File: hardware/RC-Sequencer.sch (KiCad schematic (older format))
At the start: 18 parts, among them J1 CH3, J2 Conn_02x05_Odd_Even, J3 Conn_02x04_Odd_Even, Q1 AO3400, Q2 AO3400, Q3 AO3400, Q4 AO3400, U1 ATtiny44-20SSU

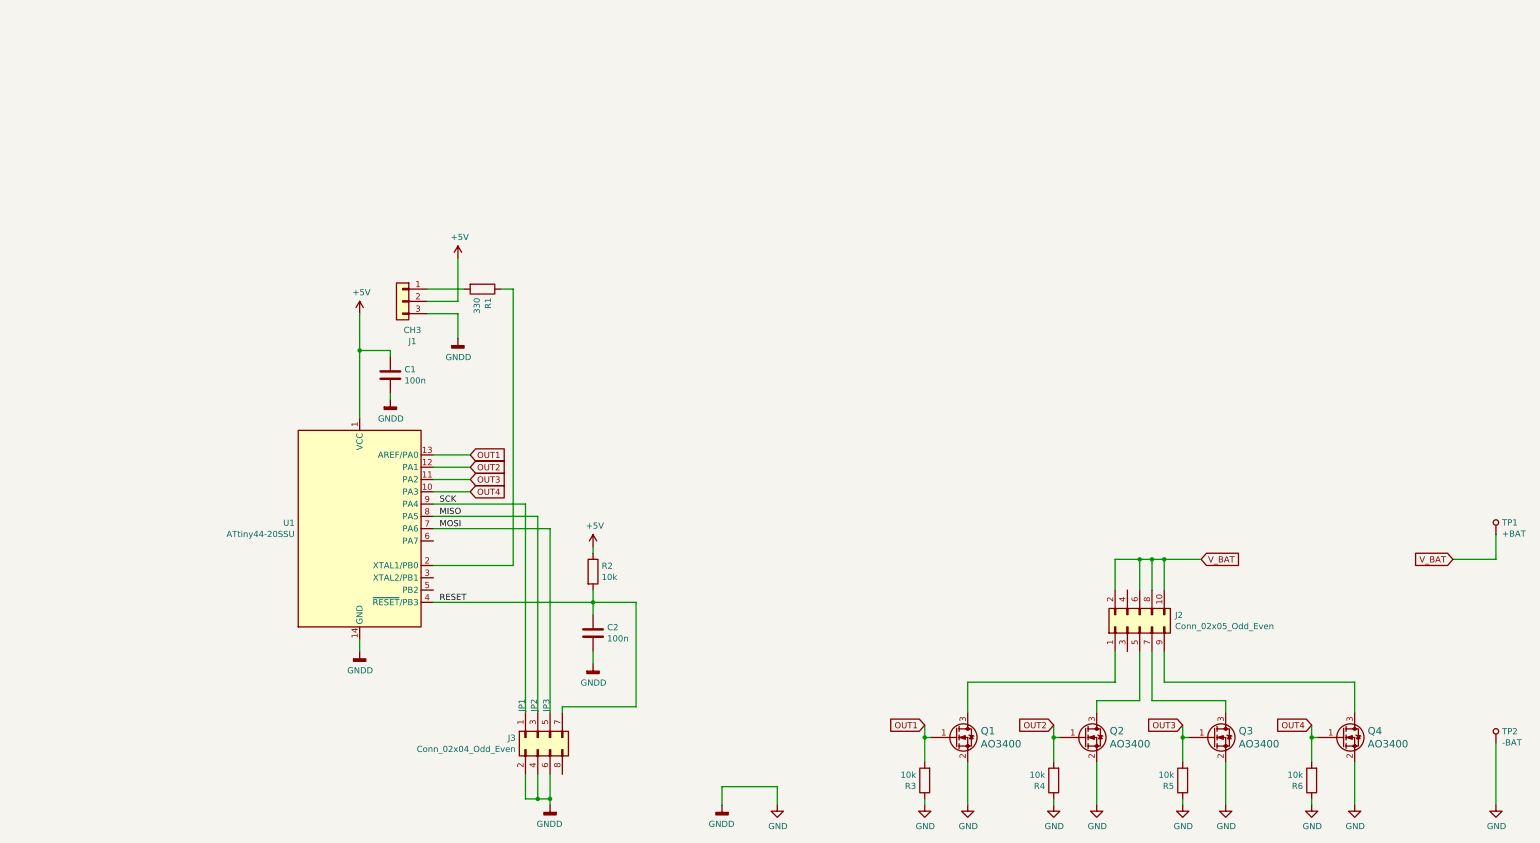
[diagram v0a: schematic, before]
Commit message: 
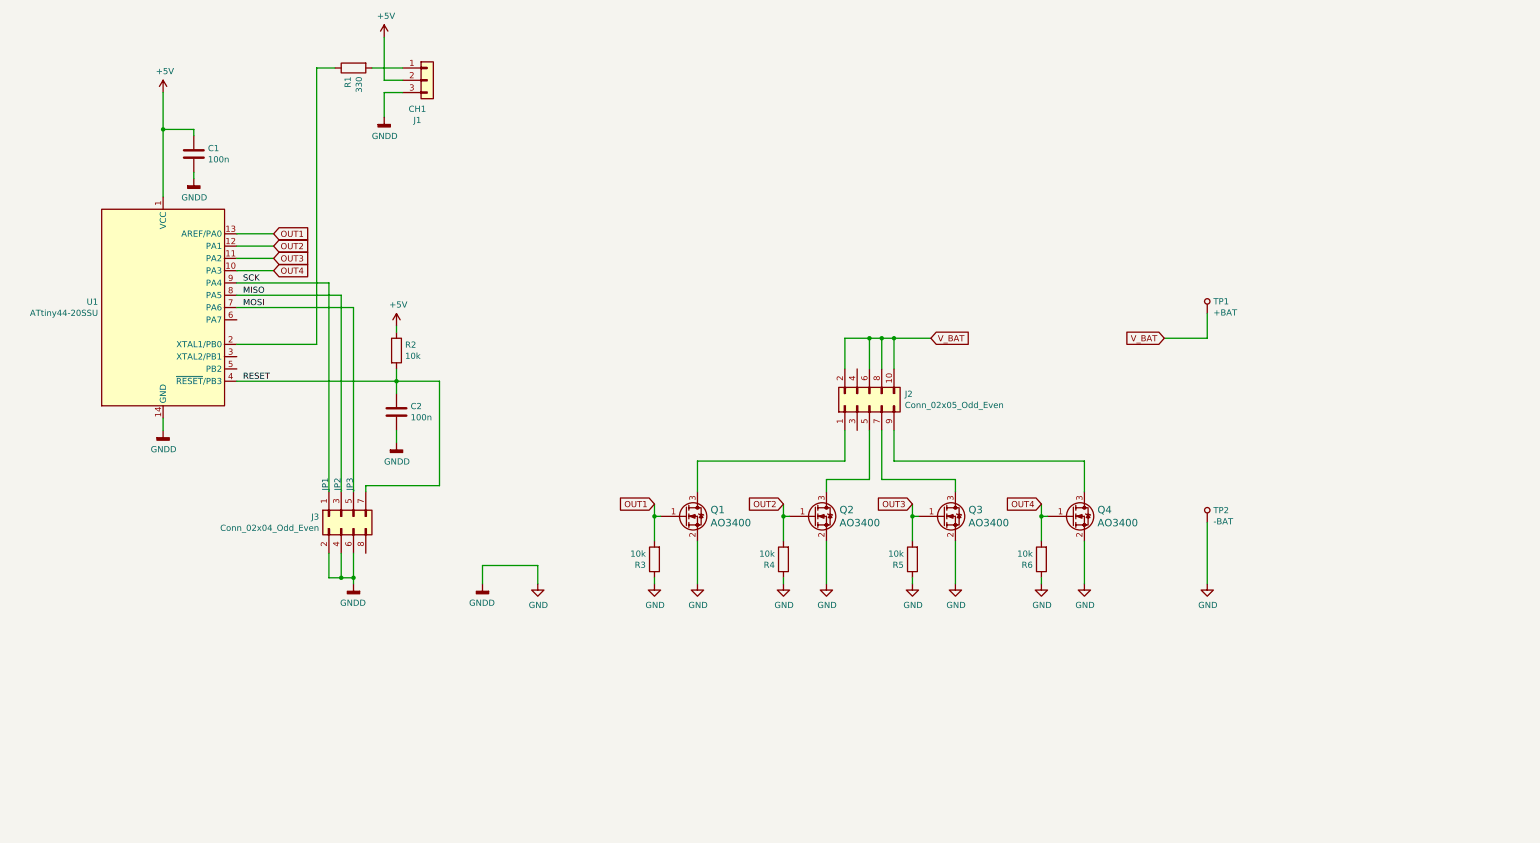
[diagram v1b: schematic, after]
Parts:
- J1: value CH3 -> CH1
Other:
- moved on the sheet: C1, C2, J1, J2, J3, Q1, Q2, Q3, Q4, R1, R2, R3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
